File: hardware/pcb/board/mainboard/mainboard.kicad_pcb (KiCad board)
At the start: 6 copper layers, 72.5 x 55 mm, 132 parts, among them J1 Conn_Coaxial, J10 USB_C_Receptacle, J11 2908-05WB-MG, J2 BATTERY_Insta_360_Ace_Pro, J3 Conn_02x35_Odd_Even_MountingP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, J4 Conn_02x40_Odd_Even_MountingP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, J5 Conn_02x40_Odd_Even_MountingP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, J6 USB_C_Receptacle, J7 Conn_01x30, J8 Conn_01x30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

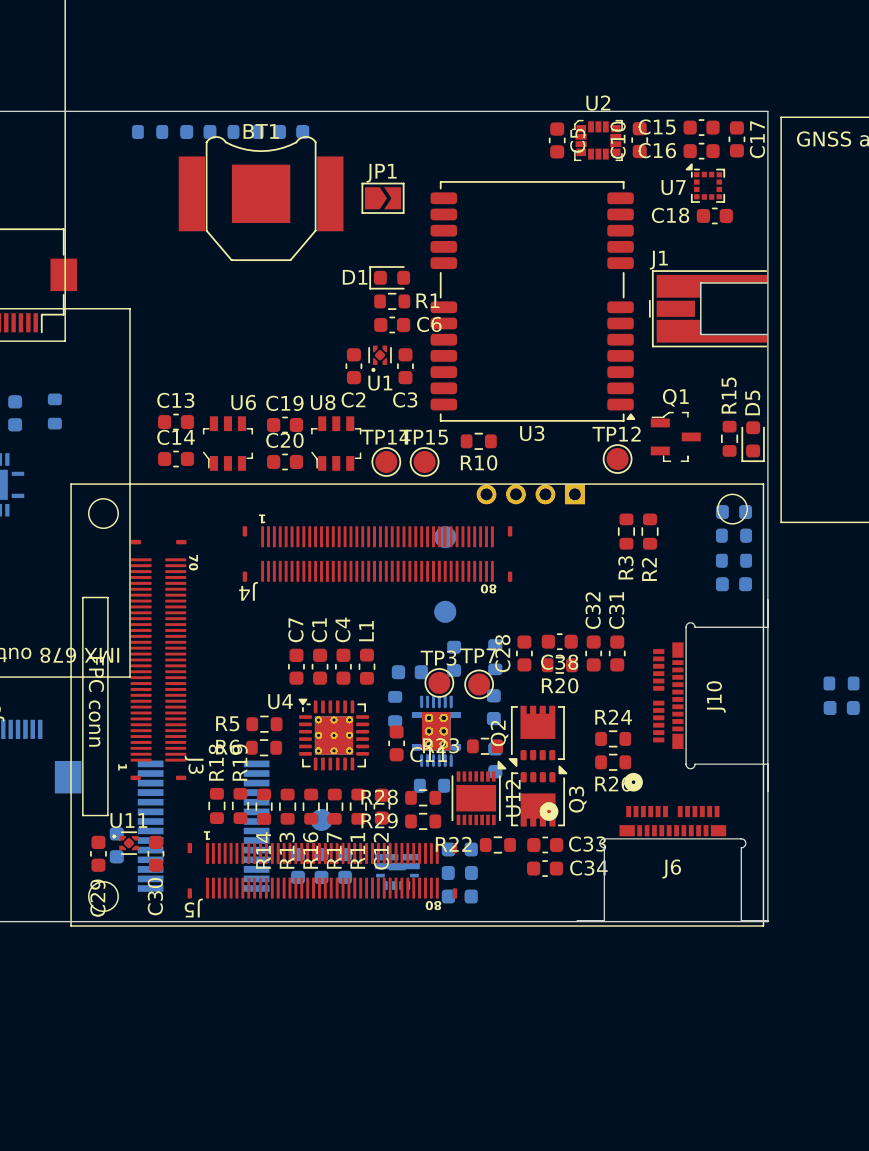
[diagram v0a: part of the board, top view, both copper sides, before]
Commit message: replace battery with dual 18350
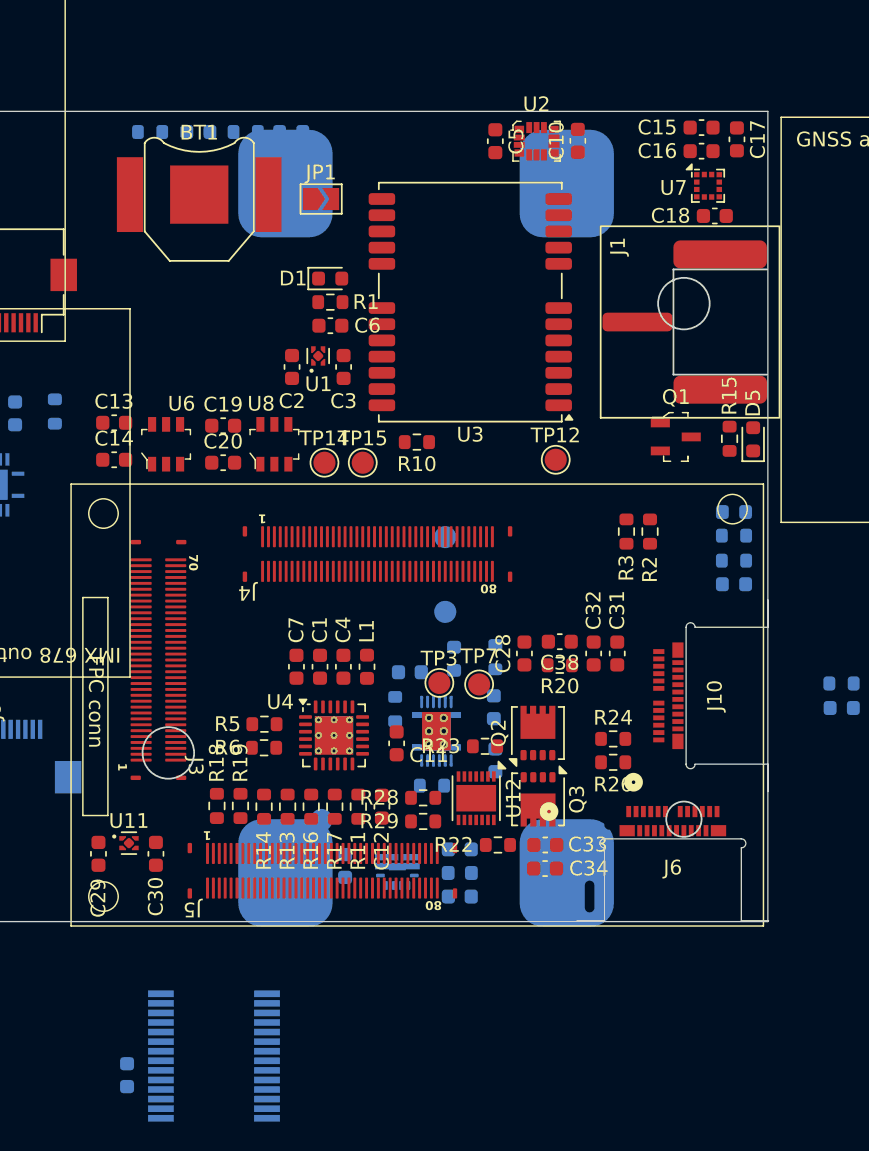
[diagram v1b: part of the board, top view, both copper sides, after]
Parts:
- removed J2: BATTERY_Insta_360_Ace_Pro, Connector_PinHeader_2.00mm:PinHeader_1x04_P2.00mm_Vertical
- added BT2: dual_18350_battery, unsurv_offline_pcb_footprints:keystone_dual_18350, B.Cu at (149.3, 128.3)
- J1: footprint Connector_Coaxial:MMCX_Molex_73415-0961_Horizontal_1.6mm-PCB -> unsurv_offline_pcb_footprints:MOLEX_SMA_0732511143
- moved C27 15.6 mm to (129.0, 165.4)
- moved U10 15.6 mm to (134.9, 164.1)
- moved C10 4.20 mm to (159.6, 102.0)
- moved C2 4.20 mm to (140.2, 117.3)
- moved C3 4.20 mm to (143.7, 117.3)
- moved D1 4.20 mm to (142.8, 111.3)
- moved TP12 4.20 mm to (158.1, 123.7)
- moved U1 4.20 mm to (142.0, 116.6)
- moved BT1 4.20 mm to (133.9, 105.7)
- moved C13 4.20 mm to (128.1, 121.1)
- moved C14 4.20 mm to (128.1, 123.7)
- moved C19 4.20 mm to (135.5, 121.3)
- moved C20 4.20 mm to (135.5, 123.8)
- moved C5 4.20 mm to (154.0, 102.0)
- moved C6 4.20 mm to (142.8, 114.5)
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
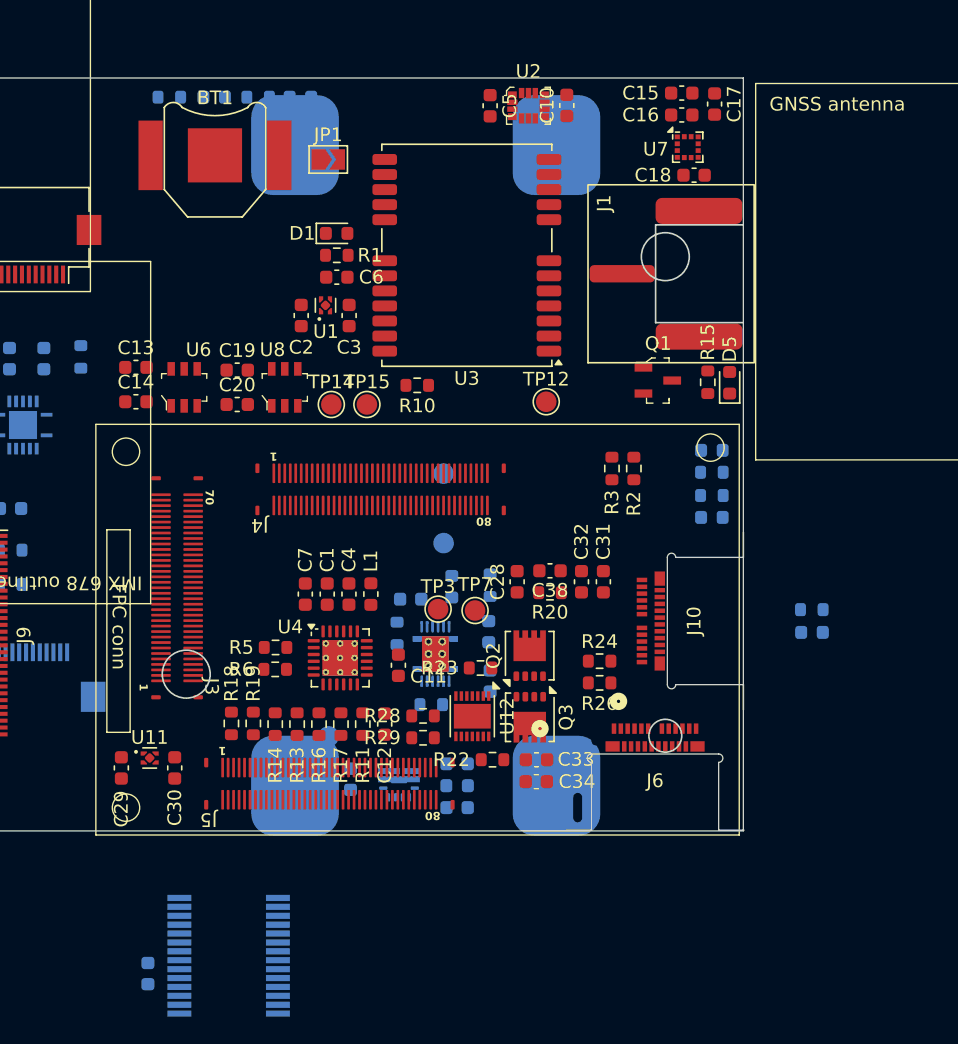
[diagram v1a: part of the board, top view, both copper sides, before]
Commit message: organize PCB around new battery holder
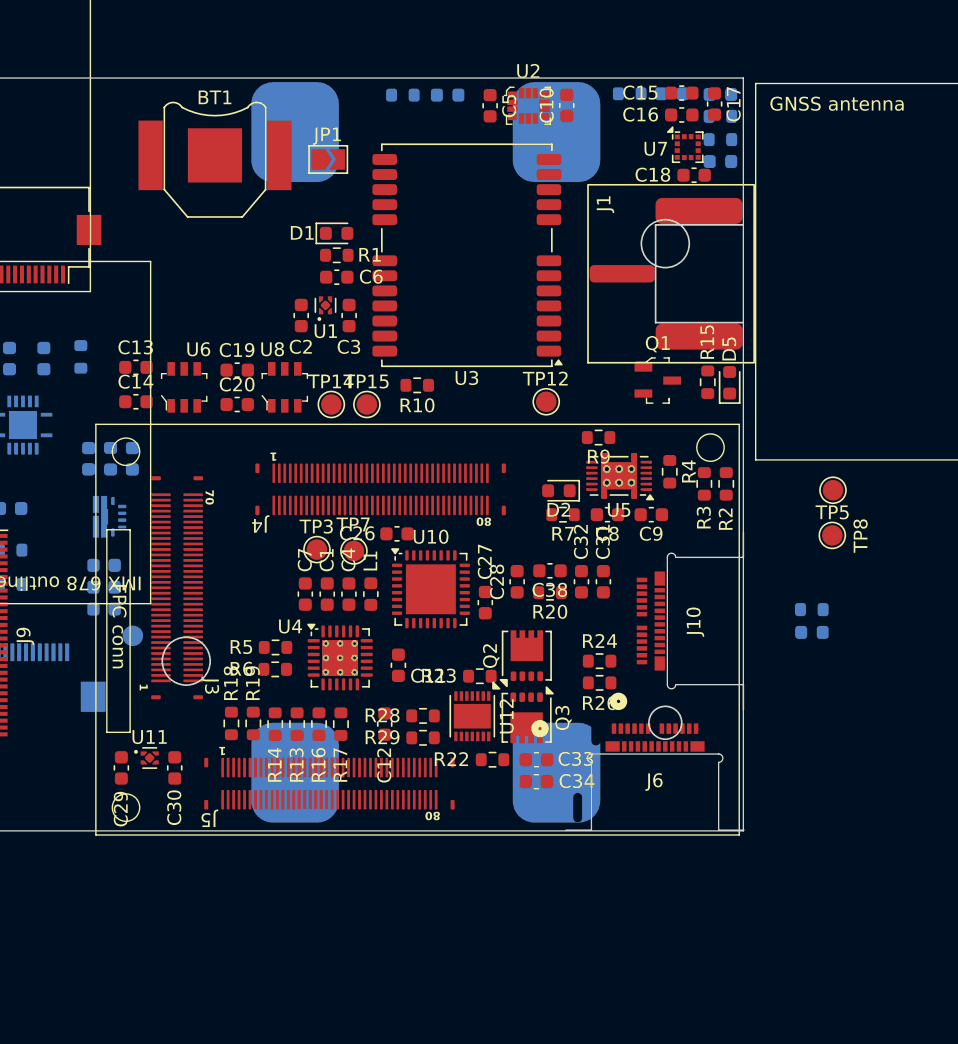
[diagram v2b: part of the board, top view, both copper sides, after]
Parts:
- removed R11: 10k, Resistor_SMD:R_0603_1608Metric
- C26, C27, C8, C9, D2, R4, R7, TP5, TP8, U5: moved to F.Cu
- R13: value 5.23k -> 10k
- R14: value 30.1k -> 10k
- R9: value 1.8M -> 10k; moved to F.Cu
- U10: footprint Package_SO:SSOP-28_5.3x10.2mm_P0.65mm -> Package_DFN_QFN:QFN-32-1EP_5x5mm_P0.5mm_EP3.65x3.65mm; moved to F.Cu
- moved C27 36.6 mm to (153.7, 138.3)
- moved C24 34.9 mm to (124.7, 127.8), turned to -90 degrees
- moved C25 34.8 mm to (127.9, 127.8), turned to -90 degrees
- moved L2 34.8 mm to (126.3, 127.8), turned to -90 degrees
- moved U10 30.6 mm to (149.7, 137.3), turned to 0 degrees
- moved U9 28.8 mm to (126.0, 132.1), turned to -90 degrees
- moved TP8 28.8 mm to (179.0, 133.4), turned to -90 degrees
- moved TP5 28.7 mm to (179.1, 130.1), turned to 180 degrees
- moved D4 27.1 mm to (167.3, 101.2)
- moved R12 27.1 mm to (164.2, 101.2)
- moved R27 26.0 mm to (170.8, 102.8)
- moved D7 26.0 mm to (170.8, 101.2)
- moved D8 26.0 mm to (170.8, 106.1)
- moved R32 26.0 mm to (170.8, 104.5)
- moved R4 24.4 mm to (167.1, 128.8), turned to -90 degrees
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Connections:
- R9 pad 1: BAT_SENSE_1V8 -> GND
- R9 pad 2: BATTERY_THERM -> Net-(U5-BIN)
- U4 pad 12: Net-(U4-VSET) -> unconnected-(U4-VSET-Pad12)
- U5 pad 10: BATTERY_THERM -> Net-(U5-BIN)
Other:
- board text removed: "BATTERY"

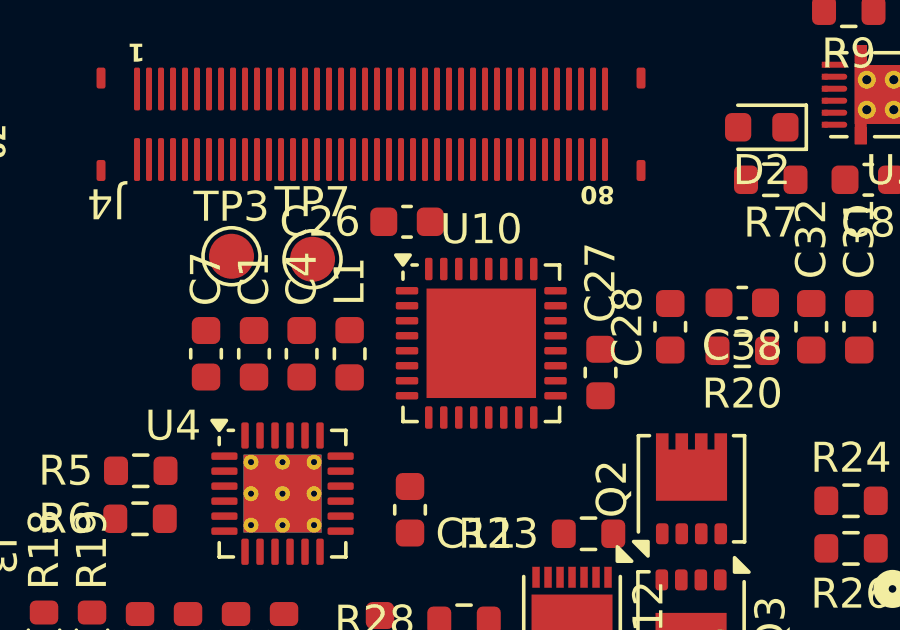
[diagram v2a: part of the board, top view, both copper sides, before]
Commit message: replace FTDI with DFN12 package
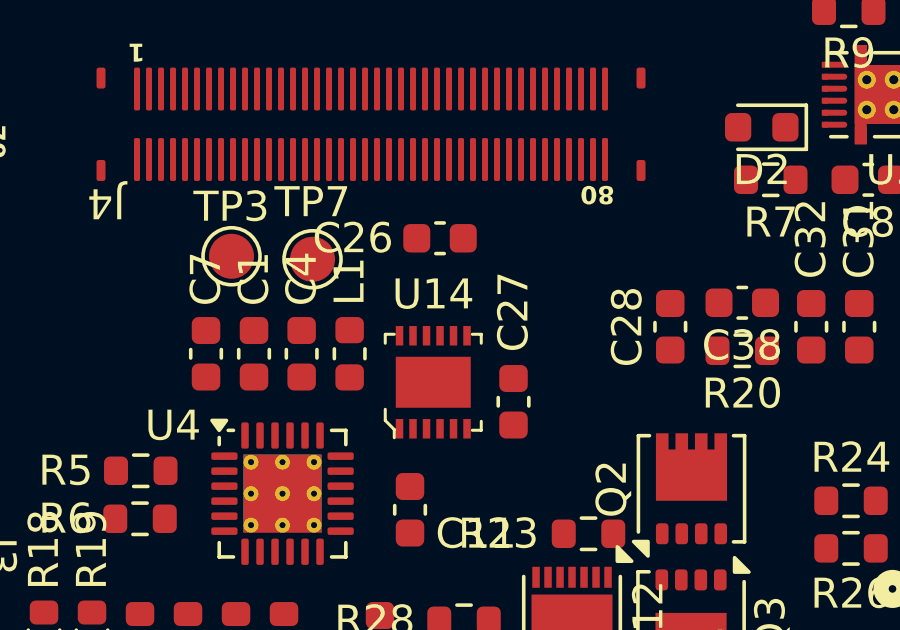
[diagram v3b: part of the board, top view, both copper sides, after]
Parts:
- removed U10: FT232RL, Package_DFN_QFN:QFN-32-1EP_5x5mm_P0.5mm_EP3.65x3.65mm
- added U14: FT234XD-R, digikey-footprints:DFN-12-1EP_3x3mm, F.Cu at (148.1, 138.7)
- moved C27 3.06 mm to (150.8, 139.3)
- moved C26 1.23 mm to (148.3, 133.8)

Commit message: update active antenna design
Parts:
- added C39: 0.1 uF, 25V, +80% - 20%, Capacitor_SMD:C_0603_1608Metric, F.Cu at (161.8, 116.9)
- added C40: 47pF, 50V, 5%, Capacitor_SMD:C_0603_1608Metric, F.Cu at (162.1, 110.1)
- added C41: 47pF, 50V, 5%, Capacitor_SMD:C_0603_1608Metric, F.Cu at (160.3, 113.4)
- added D9: PGB1010402KR, Diode_SMD:D_0402_1005Metric, F.Cu at (164.0, 112.3)
- added L3: 33 nH, 100 mhz, 5%, Inductor_SMD:L_0402_1005Metric, F.Cu at (162.1, 112.5)
- added R11: 10, 5%, 0,25W, Resistor_SMD:R_0603_1608Metric, F.Cu at (160.5, 110.1)
- moved BT2 3.05 mm to (152.3, 127.3)
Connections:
- U3 pad 11: Net-(J1-In) -> RF_IN
- U3 pad 9: unconnected-(U3-VCC_RF-Pad9) -> VCC_RF

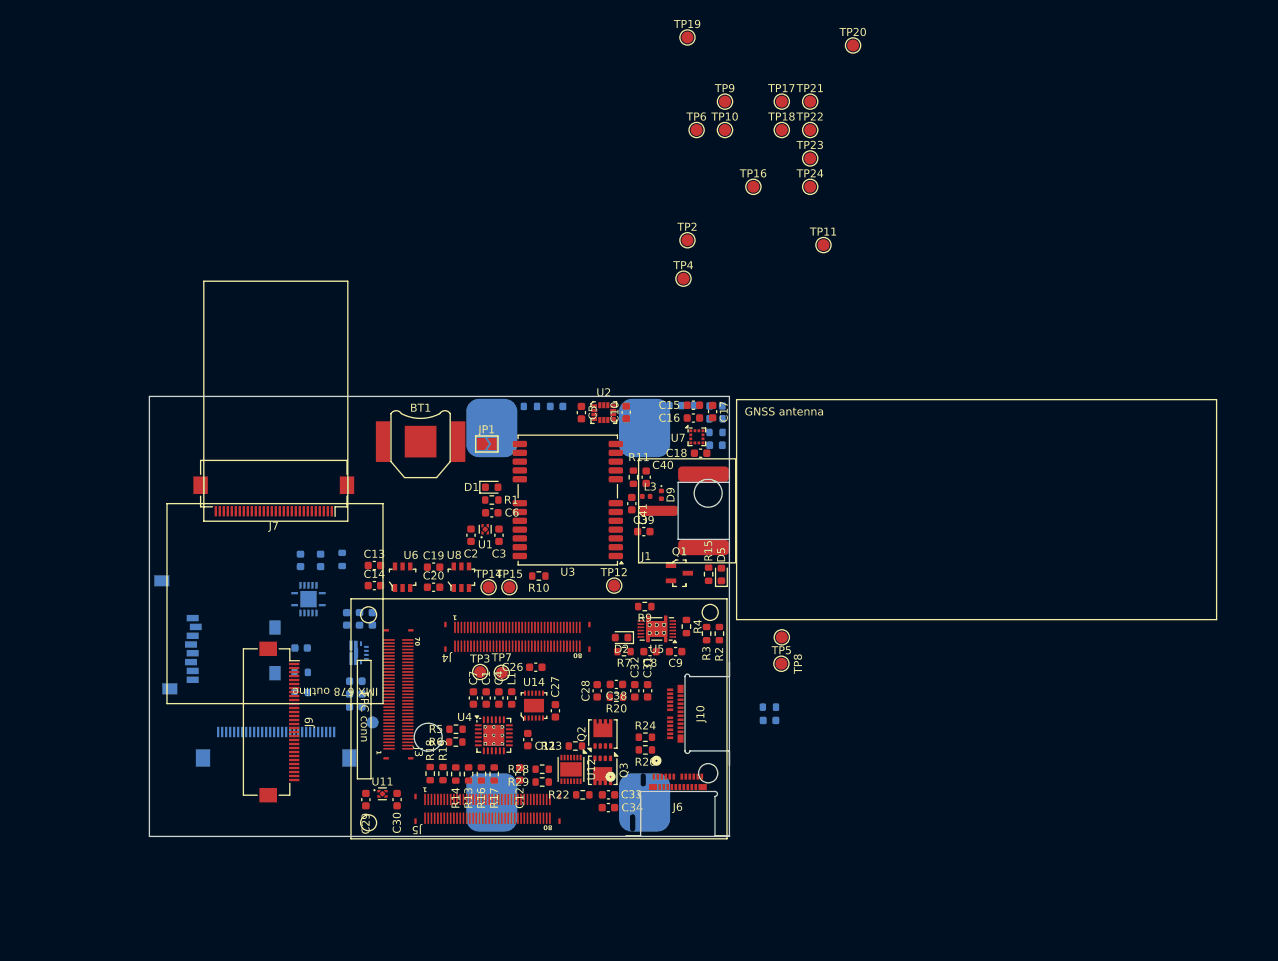
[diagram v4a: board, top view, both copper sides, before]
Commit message: update SMA receptable
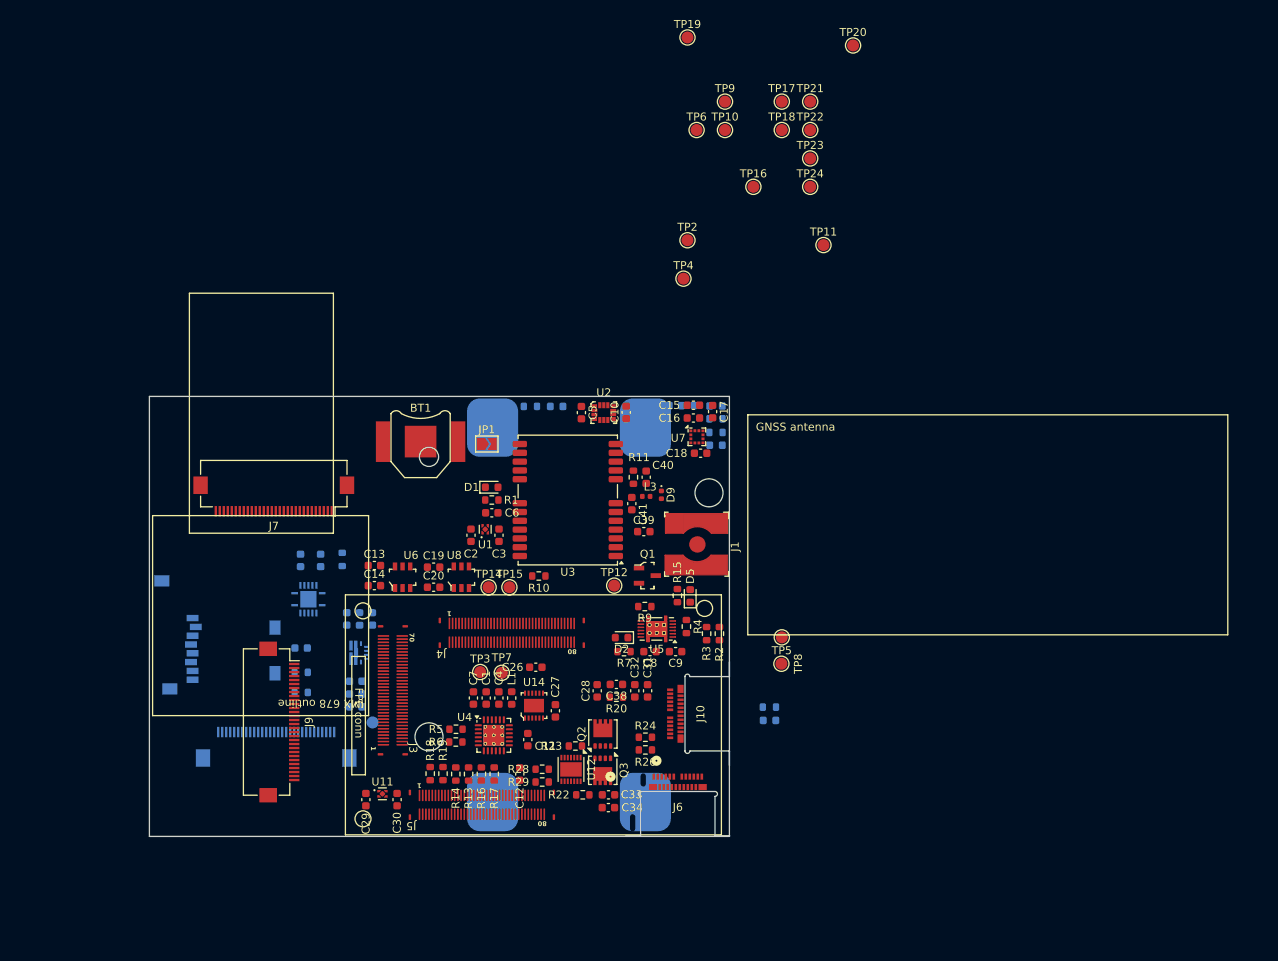
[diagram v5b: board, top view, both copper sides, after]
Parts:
- J1: footprint unsurv_offline_pcb_footprints:MOLEX_SMA_0732511143 -> unsurv_offline_pcb_footprints:RF_SMA_Receptical_Vertical_CONSMA002-SMD-G
- moved J1 4.77 mm to (168.4, 118.5), turned to -90 degrees
- moved R15 4.73 mm to (166.0, 124.9)
- moved D5 4.73 mm to (167.6, 124.9)
- moved Q1 4.01 mm to (162.2, 122.4)
- moved J3 0.86 mm to (130.4, 136.7)
- moved J4 0.86 mm to (145.3, 129.6)
- moved J5 0.86 mm to (141.6, 151.1)
- moved BT2 0.11 mm to (152.4, 127.3), turned to 90 degrees
